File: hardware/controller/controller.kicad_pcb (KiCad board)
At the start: 2 copper layers, 100 x 100 mm, 134 parts, among them J1 230V~, J10 FAN, J2 LOAD, J3 DISPLAY, J4 PANEL, J5 TC top, J6 TC bot, J7 USB-C, J9 UART, Q1 AO3401A, Q2 BSS138, Q3 IRLML6346, Q4 IRLML6346, Q5 IRLML6346, Q6 AO3401A, Q7 IRLML6346, Q8 BSS138, SW1 RESET, SW2 BOOT, U1 IRM-10-5, U10 USBLC6-2SC6, U11 USBLC6-2SC6, U12 USBLC6-2SC6, U2 AP7361C-33E, U3 ESP32-S3-WROOM-1U-N8, U4 USBLC6-2SC6, U5 MAX31856MUD+, U6 MAX31856MUD+, U7 SN74LVC74AD, U8 TPS3828-33DBV, U9 TC6501P065

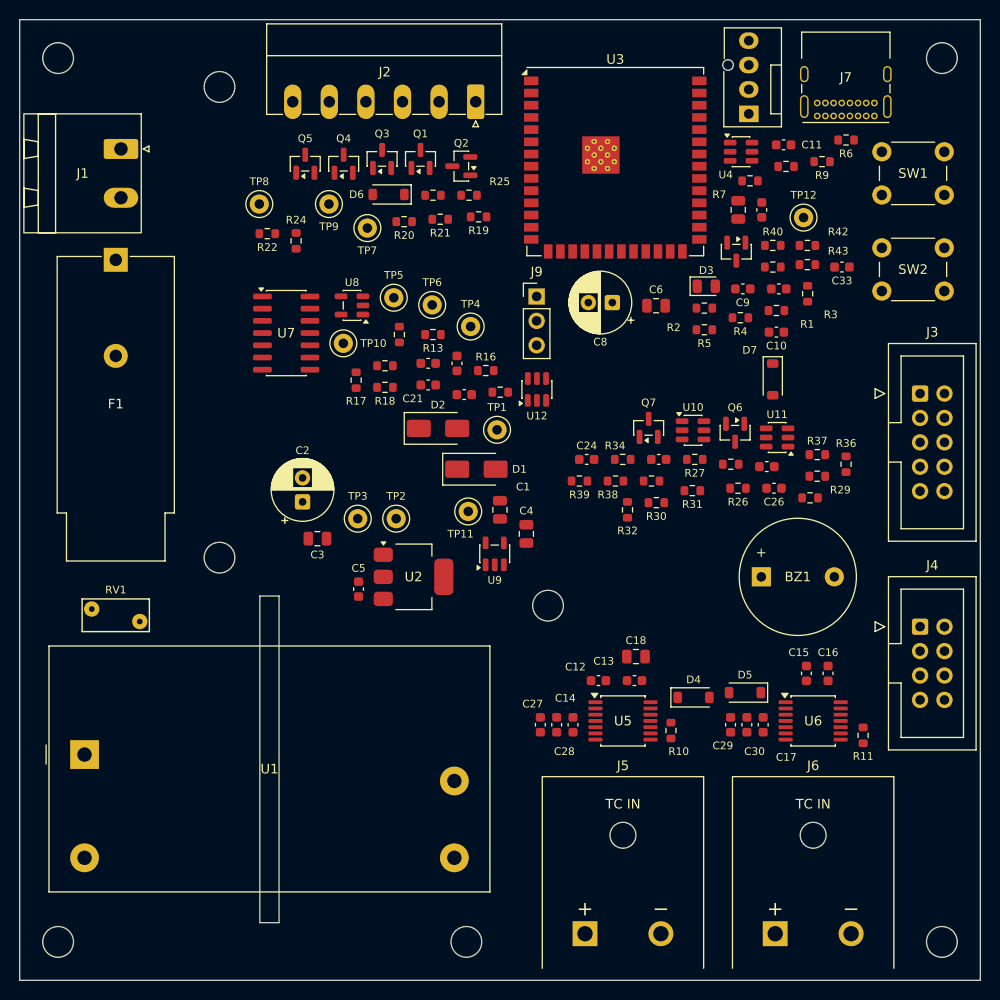
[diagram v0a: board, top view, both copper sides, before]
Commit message: feat(hardware): controller REV A routed except 10 GND islands (T021)
- mains copper routed by hand (top, 1 mm, locked); RV1 turned by 180
  degrees so N runs along the left edge and L on the right without
  crossing; 6 mm to low voltage, 3 mm L-N, 3 mm to edge, 6 mm to H5/H6
- GND zones top and bottom over the low-voltage area, stitching vias on
  a 3 mm grid, SMD pads solid, THT pads with thermal relief
- signals routed with Freerouting 1.9.0, +5V_PSU and TFT_RST by script
- net class USB (VBUS, USB_DP/DN, CC1/2: 0.25 mm, 0.15 mm clearance)
  for the 0.85 mm pad pitch of J7, board minimum clearance 0.15 mm;
  same in make_project.py
- silkscreen: 230 V warning, L/N, project name, REV A, pinouts at J2,
  J3, J4, J9, J10, labels at J5/J6/J7
- docs: Freerouting findings in docs/werkzeuge-pcb.md, T021 status;
  J5/J6 colour in contracts/connectors.md

DRC with schematic parity: no clearance, net or parity violations;
open: 10 unconnected GND islands on the top layer, 10 starved thermals
at J7/J9/J3, 2 silk edge warnings at U1. check_schematic: 0 errors.

Co-Authored-By: Claude Opus 5.5 <noreply@anthropic.com>
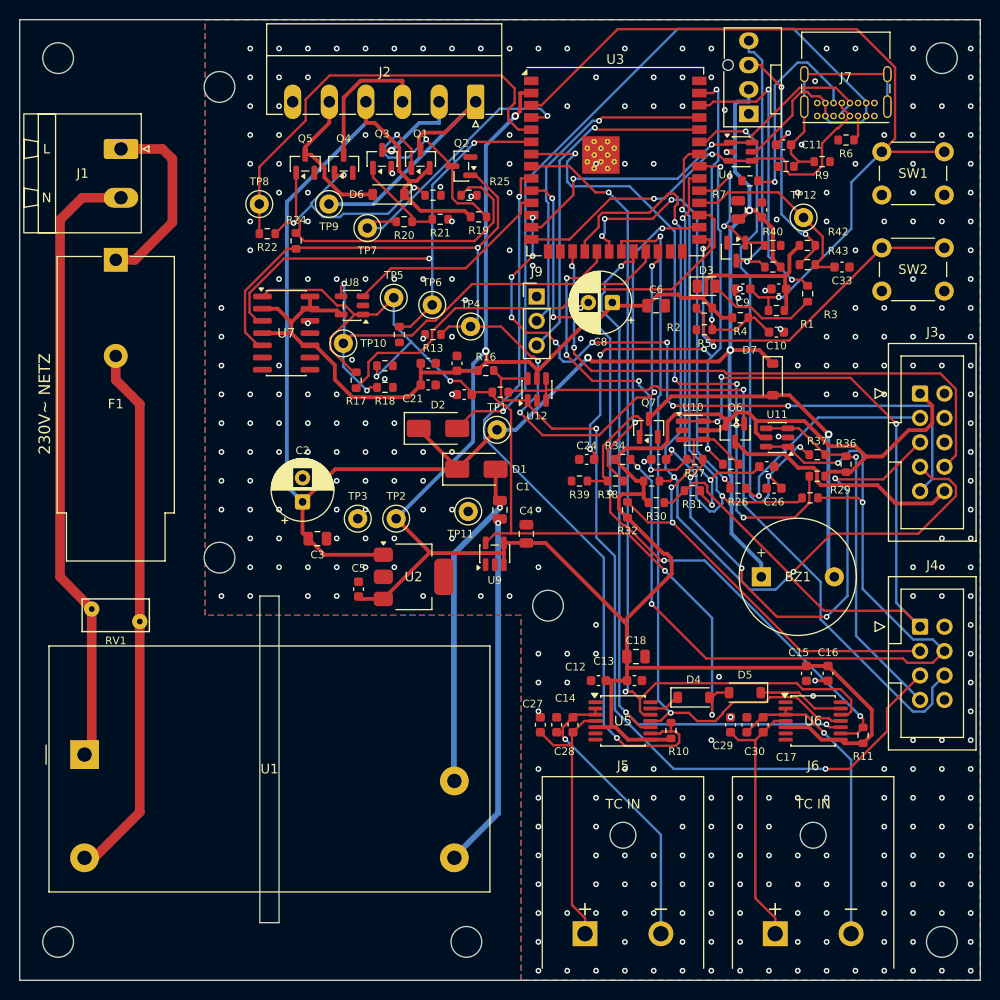
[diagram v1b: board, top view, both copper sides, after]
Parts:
- moved RV1 5.17 mm to (12.5, 62.6), turned to 180 degrees
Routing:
- net +3V3: track 0.00 -> 327.0 mm, vias 0 -> 2
- net +5V: track 0.00 -> 207.4 mm, vias 0 -> 3
- net CLR: track 0.00 -> 104.1 mm, vias 0 -> 4
- net LATCH_Q: track 0.00 -> 101.2 mm, vias 0 -> 5
- net VBUS: track 0.00 -> 95.1 mm, vias 0 -> 1
- net TC_MOSI: track 0.00 -> 92.2 mm, vias 0 -> 2
- net TFT_CS: track 0.00 -> 91.9 mm, vias 0 -> 3
- net Net-(J4-Pin_4): track 0.00 -> 90.9 mm, vias 0 -> 4
- net Net-(J4-Pin_5): track 0.00 -> 87.2 mm, vias 0 -> 2
- net Net-(J4-Pin_1): track 0.00 -> 85.1 mm, vias 0 -> 3
- net EN: track 0.00 -> 83.2 mm, vias 0 -> 1
- net TC_CS_BOT: track 0.00 -> 78.7 mm, vias 0 -> 6
- net TC_CS_TOP: track 0.00 -> 78.5 mm, vias 0 -> 2
- net TC_MISO: track 0.00 -> 78.2 mm, vias 0 -> 2
- net TC_SCK: track 0.00 -> 77.1 mm, vias 0 -> 3
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- added copper zone on B.Cu, net GND
- added copper zone on F.Cu, net GND
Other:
- board text added: "+5V"
- board text added: "+5V_SSR"
- board text added: "1 3V3 2 GND"
- board text added: "1 ENC_A 2 GND"
- board text added: "230V~"
- board text added: "230V~ NETZ"
- board text added: "3 ENC_B 4 SW"
- board text added: "3 SCK 4 GND"
- board text added: "5 MOSI 6 GND"
- board text added: "5 STOP_NC 6 RET"
- board text added: "7 CS 8 DC"
- board text added: "7 STOP_NO 8 GND"
- board text added: "9 RST 10 BL"
- board text added: "ACHTUNG 230V~"
- board text added: "GND"
- board text added: "J10 FAN 5V"
- board text added: "J2 LAST"
- board text added: "J3 DISPLAY"
- board text added: "J4 BEDIENTEIL"
- board text added: "J5 TC OBEN"
- board text added: "J6 TC UNTEN"
- board text added: "J7 USB-C"
- board text added: "J9 UART"
- board text added: "L"
- board text added: "N"
- board text added: "OFEN-CONTROLLER"
- board text added: "PWM"
- board text added: "RELAIS-"
- board text added: "REV A 2026-10"
- board text added: "RX"
- board text added: "SSR_O-"
- board text added: "SSR_U-"
- board text added: "TACH"
- board text added: "TX"
- board text added: "nur mit Netzabdeckung betreiben"

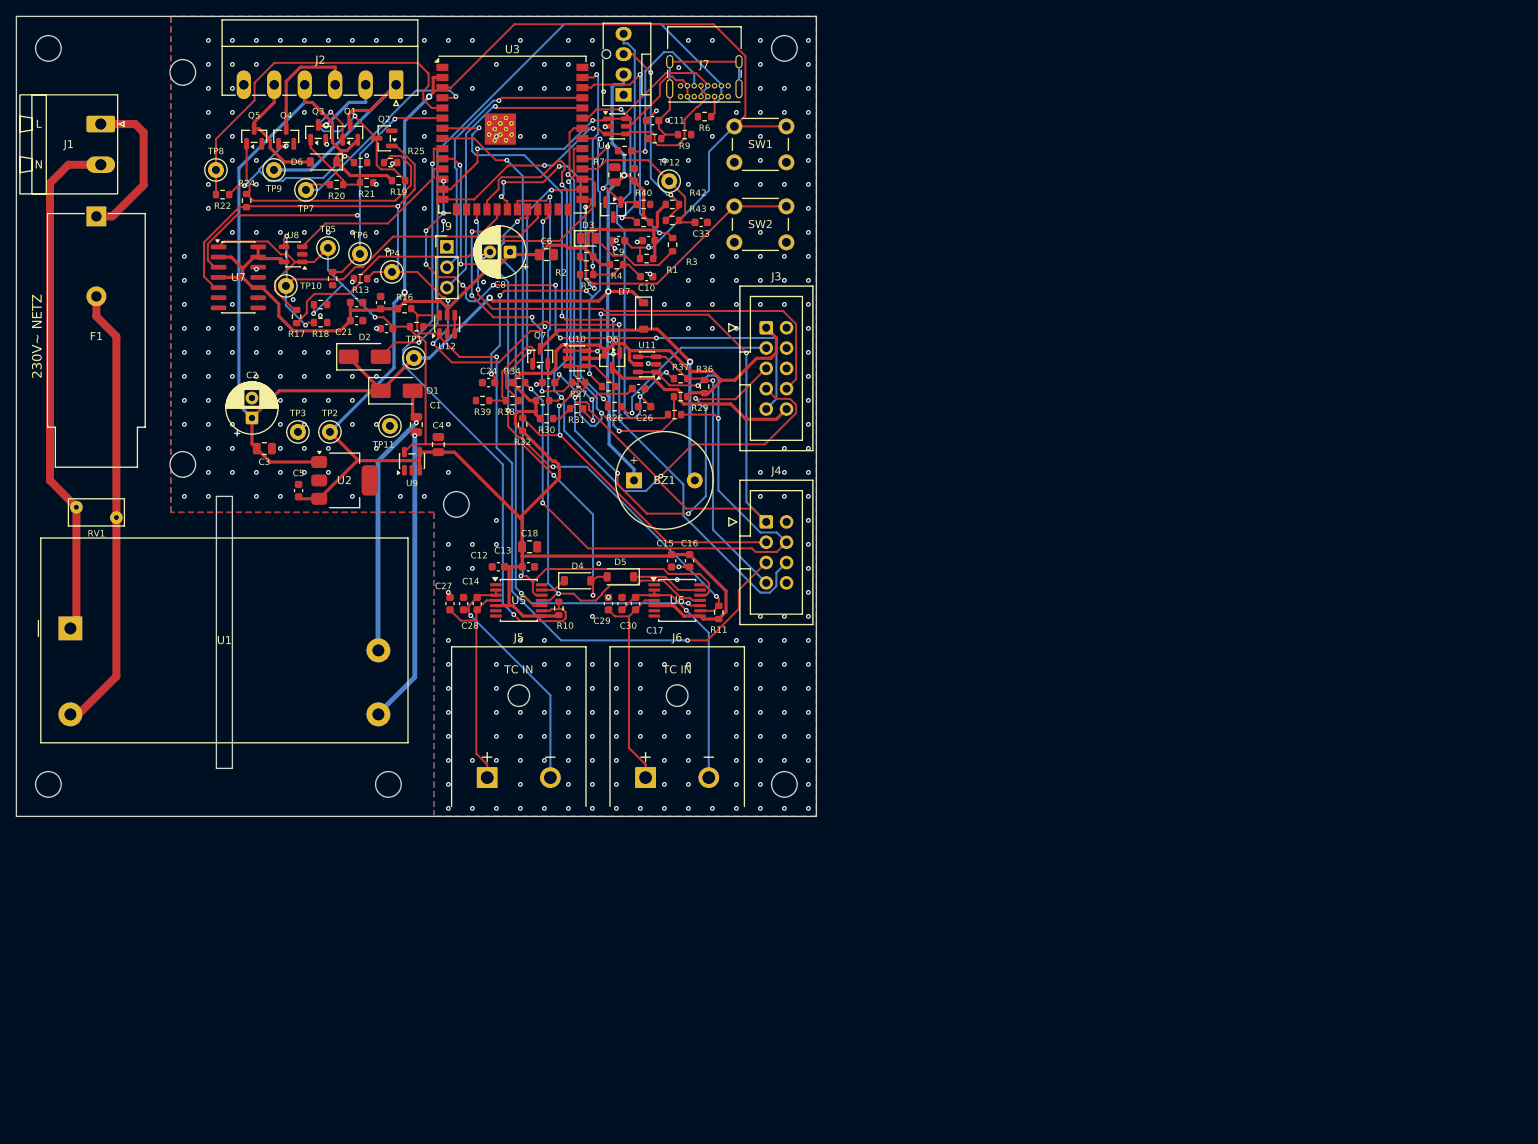
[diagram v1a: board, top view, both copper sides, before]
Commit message: feat(hardware): JST XH connectors, re-placement and re-route, open fuse holder (T087, T021)
Connectors (T087, research R9/R10, contracts/connectors.md):
- J3 display JST XH 1x10 (same pin order as the IDC 2x5)
- J4 encoder JST XH 1x5 (A, GND, B, SW, GND), new J11 stop button
  JST XH 1x4 directly on the main board; an unplugged stop connector
  opens the NC loop like a pressed stop button
- encoder carrier: J1 JST XH 1x5, J2 (stop wires) removed
- schematic wire chains of the old connectors replaced by labels,
  connectivity checked pin by pin; ref netlists re-exported

Layout:
- XH connectors at the right edge, RESET/BOOT moved inside
- decoupling capacitors next to their IC pins (LDO 2.6/2.9 mm,
  MAX31856 2.3-3.7 mm, U7/U8/U9 2.2-4.3 mm, ESP32 5.1 mm)
- EMC: flyback diode D7 at the buzzer, 33 ohm SPI resistors at the
  module pins, C1 on the IRM-10-5 output path, thermal vias at the LDO
- re-routed with Freerouting 1.9.0 (2.5.0 compared and rejected),
  GND stitching and isolated GND groups connected
- manual rework by the user: USB D+/D- through the ESD array U4 at the
  connector, tightly coupled, CC2 connected, U4 pin 2 GND connected
- COV1 restored after an accidental delete, dangling stubs removed
- F1: Schurter OGN 0031.8201 open fuse holder instead of the FAB, whose
  carrier is pulled out axially and was blocked by RV1/IRM-10-5;
  L_FUSED re-routed

DRC with schematic parity: 0 errors, 0 unconnected (2 silk edge
warnings from the U1 footprint); check_schematic 0 errors for both
boards; ERC only the documented SDO exclusion.

Co-Authored-By: Claude Opus 5.5 <noreply@anthropic.com>
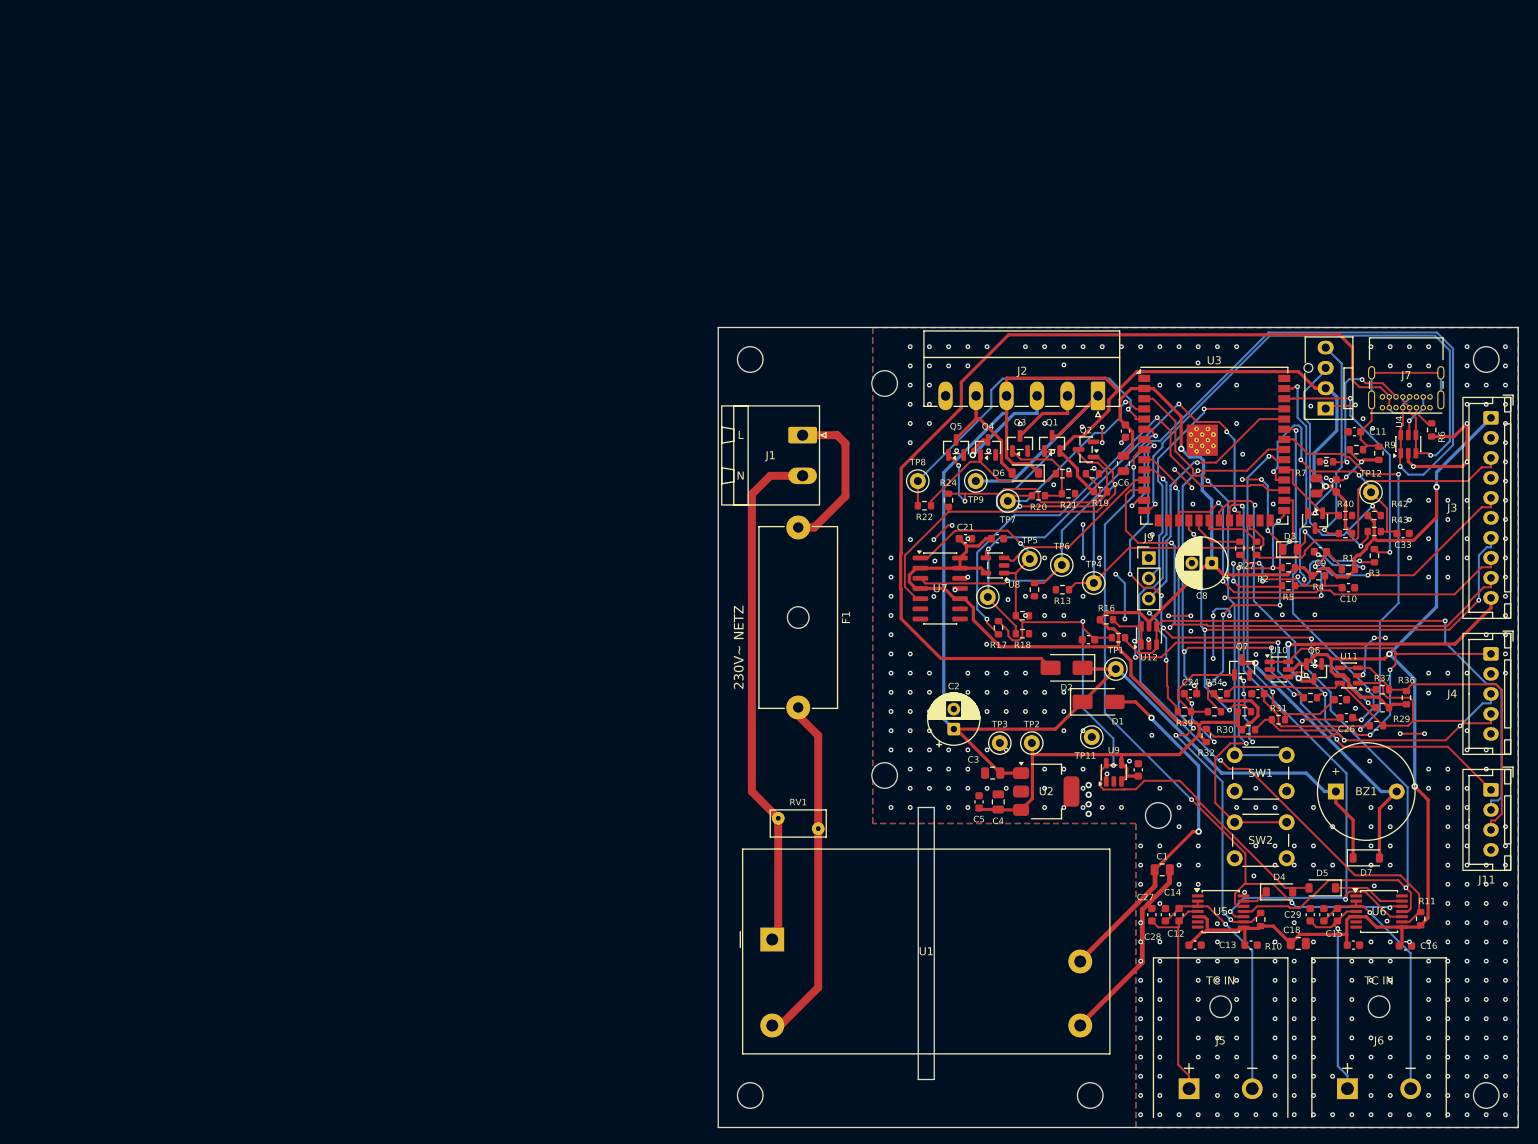
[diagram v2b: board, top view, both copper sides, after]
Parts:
- added J11: STOP, Connector_JST:JST_XH_B4B-XH-A_1x04_P2.50mm_Vertical, F.Cu at (184.3, 96.7)
- F1: footprint Fuse:Fuseholder_Cylinder-5x20mm_Schurter_FAB_0031-355x_Horizontal_Closed -> Fuse:Fuseholder_Cylinder-5x20mm_Schurter_0031_8201_Horizontal_Open
- J3: footprint Connector_IDC:IDC-Header_2x05_P2.54mm_Vertical -> Connector_JST:JST_XH_B10B-XH-A_1x10_P2.50mm_Vertical
- J4: value PANEL -> ENCODER; footprint Connector_IDC:IDC-Header_2x04_P2.54mm_Vertical -> Connector_JST:JST_XH_B5B-XH-A_1x05_P2.50mm_Vertical
- moved D7 112.9 mm to (168.7, 105.2), turned to 0 degrees
- moved C19 111.3 mm to (140.2, 94.2)
- moved C1 108.6 mm to (143.2, 106.7), turned to 0 degrees
- moved C18 108.1 mm to (160.2, 115.9)
- moved U4 106.6 mm to (174.0, 53.5), turned to 90 degrees
- moved C13 102.0 mm to (154.3, 116.1)
- moved C16 101.6 mm to (173.6, 116.2), turned to 0 degrees
- moved SW1 100.4 mm to (152.3, 92.3)
- moved C3 99.7 mm to (122.0, 94.6), turned to 180 degrees
- moved SW2 99.2 mm to (152.3, 100.7)
- moved C12 99.1 mm to (147.3, 116.1), turned to 0 degrees
- moved R6 99.0 mm to (176.9, 51.7), turned to -90 degrees
- moved C15 97.8 mm to (167.1, 116.1), turned to 0 degrees
- moved C25 96.8 mm to (155.2, 84.7)
- moved J10 96.1 mm to (163.7, 49.0)
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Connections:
- net Net-(J3-Pin_3) renamed /Steuerung und Messung/TFT_SCK
- net Net-(J3-Pin_5) renamed /Steuerung und Messung/TFT_MOSI
- net Net-(J4-Pin_1) renamed /Steuerung und Messung/ENC_A_IN
- net Net-(J4-Pin_3) renamed /Steuerung und Messung/ENC_B_IN
- net Net-(J4-Pin_4) renamed /Steuerung und Messung/ENC_SW_IN
- J4 pad 5: Net-(J4-Pin_5) -> GND
- R16 pad 2: Net-(J4-Pin_5) -> /Steuerung und Messung/STOP_NC_OUT
- R36 pad 2: Net-(J4-Pin_7) -> /Steuerung und Messung/STOP_NO_IN
- R37 pad 1: Net-(J4-Pin_7) -> /Steuerung und Messung/STOP_NO_IN
- U11 pad 3: Net-(J4-Pin_7) -> /Steuerung und Messung/STOP_NO_IN
- U11 pad 4: Net-(J4-Pin_7) -> /Steuerung und Messung/STOP_NO_IN
- U12 pad 1: Net-(J4-Pin_5) -> /Steuerung und Messung/STOP_NC_OUT
- U12 pad 6: Net-(J4-Pin_5) -> /Steuerung und Messung/STOP_NC_OUT
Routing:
- net GND: track 46.0 -> 159.6 mm, vias 319 -> 476
- net Net-(J4-Pin_5): track 87.2 -> 0.00 mm, vias 2 -> 0
- net /Steuerung und Messung/STOP_NC_OUT: track 0.00 -> 65.0 mm, vias 0 -> 4
- net +3V3: track 327.0 -> 370.7 mm, vias 2 -> 4
- net /Steuerung und Messung/ENC_SW_IN: track 90.9 -> 48.2 mm, vias 4 -> 0
- net USB_DN: track 43.0 -> 84.9 mm
- net /Steuerung und Messung/STOP_NO_IN: track 0.00 -> 40.6 mm
- net Net-(J4-Pin_7): track 38.6 -> 0.00 mm, vias 1 -> 0
- net TFT_SCK_MCU: track 44.9 -> 7.66 mm, vias 4 -> 0
- net USB_DP: track 44.1 -> 76.4 mm
- net VBUS: track 95.1 -> 126.7 mm
- net /Steuerung und Messung/ENC_A_IN: track 85.1 -> 56.1 mm, vias 3 -> 2
- net TFT_MOSI_MCU: track 35.6 -> 6.83 mm, vias 4 -> 0
- net +5V: track 207.4 -> 226.2 mm, vias 3 -> 1
- net TFT_CS: track 91.9 -> 73.7 mm, vias 3 -> 4
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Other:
- board text added: "1 3V3"
- board text added: "1 ENC_A"
- board text added: "1 NC_OUT"
- board text added: "10 BL"
- board text added: "2 GND"
- board text added: "2 NC_RET"
- board text added: "3 ENC_B"
- board text added: "3 NO"
- board text added: "3 SCK"
- board text added: "4 GND"
- board text added: "4 SW"
- board text added: "5 GND"
- board text added: "5 MOSI"
- board text added: "6 GND"
- board text added: "7 CS"
- board text added: "8 DC"
- board text added: "9 RST"
- board text added: "J11 STOPP"
- board text added: "J4 ENCODER"
- board text removed: "1 3V3 2 GND"
- board text removed: "1 ENC_A 2 GND"
- board text removed: "3 ENC_B 4 SW"
- board text removed: "3 SCK 4 GND"
- board text removed: "5 MOSI 6 GND"
- board text removed: "5 STOP_NC 6 RET"
- board text removed: "7 CS 8 DC"
- board text removed: "7 STOP_NO 8 GND"
- board text removed: "9 RST 10 BL"
- board text removed: "J4 BEDIENTEIL"

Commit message: feat(hardware): test point groups labelled, TP11 removed, USB shield option R9 DNP
- TP11 (second GND test point) removed, TP1 GND / TP2 3V3 / TP3 5V in a
  new order (user); contracts/connectors.md and controller.ref.net updated
- top silkscreen groups: Versorgung (TP1-3), Freigabe (TP4-6),
  SSR (TP7-9), Last-Relais; test point signal names next to the pads
- small layout optimisations; a GND via under TP4 (short to LATCH_Q) and
  a loose GND via removed, Q3 source re-connected to GND
- USB shield: R9 (0 ohm) marked DNP, shield to GND via R8 1M || C11 4.7n
- editor default pad size in the project file (user)

DRC with schematic parity: 0 errors, 0 unconnected (2 silk edge
warnings from the U1 footprint); GND copper is one connected group;
check_schematic 0 errors for both boards; ERC only the documented SDO
exclusion.

Co-Authored-By: Claude Opus 5.5 <noreply@anthropic.com>
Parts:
- removed the TP3 at (122.9, 90.8)
- moved TP1 10.8 mm to (123.7, 91.3)
- moved TP3 10.4 mm to (133.5, 91.2)
- moved TP4 2.38 mm to (134.5, 68.5)
- moved TP2 1.67 mm to (128.5, 91.3)
- moved TP5 0.75 mm to (126.7, 68.6)
- moved R12 0.22 mm to (127.3, 71.9)
- moved D1 0.21 mm to (135.3, 85.5)
- renumbered TP11 to TP1, TP1 to TP3
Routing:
- net Net-(Q1-G): track 34.3 -> 40.4 mm
- net +5V: track 226.2 -> 231.6 mm, vias 1 -> 2
- net GND: track 159.6 -> 161.4 mm, vias 476 -> 471
- net SSR_TOP_N: track 9.30 -> 8.01 mm
- net LATCH_Q: track 86.7 -> 85.7 mm
- net Net-(Q5-G): track 31.8 -> 30.8 mm
- net /Steuerung und Messung/ENC_SW_IN: track 48.2 -> 47.3 mm
- net +3V3: track 370.7 -> 369.9 mm
- net HEAT_BOT: track 41.3 -> 42.1 mm
- net /Steuerung und Messung/TFT_MOSI: track 42.6 -> 41.9 mm
- net TFT_DC: track 53.5 -> 52.8 mm
- net /Steuerung und Messung/TFT_SCK: track 39.1 -> 38.4 mm
- net /Steuerung und Messung/ENC_B_IN: track 55.8 -> 55.2 mm
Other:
- board text added: "3V3"
- board text added: "5V"
- board text added: "5V_SSR"
- board text added: "ARM"
- board text added: "CLR"
- board text added: "Display"
- board text added: "Encoder"
- board text added: "FAN"
- board text added: "FAN_TACH"
- board text added: "Freigabe"
- board text added: "H_BOT"
- board text added: "H_TOP"
- board text added: "LATCH_Q"
- board text added: "Last-Relais"
- board text added: "SSR"
- board text added: "Stop Btn"
- board text added: "TC Oben"
- board text added: "TC Unten"
- board text added: "UART"
- board text added: "Versorgung"
